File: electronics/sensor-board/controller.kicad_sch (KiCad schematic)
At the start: 22 parts

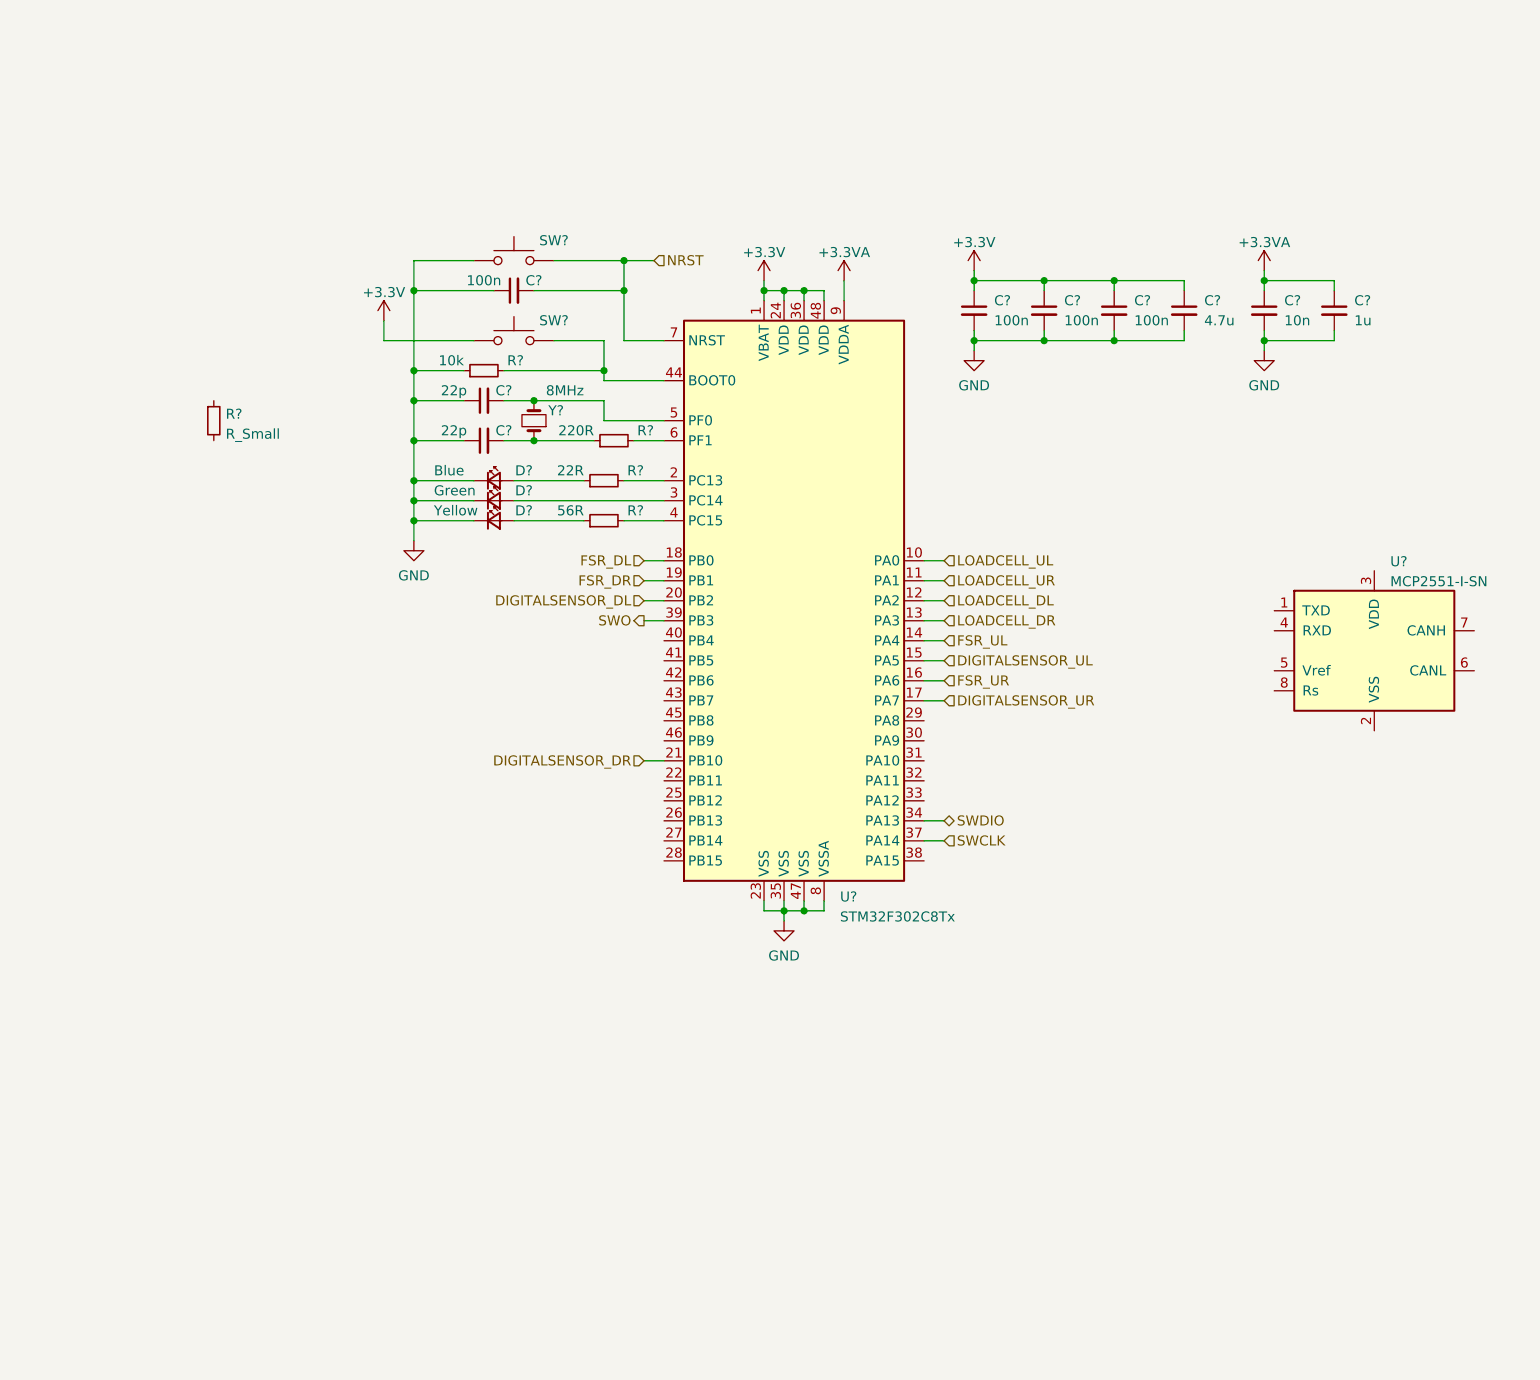
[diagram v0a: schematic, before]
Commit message: Finish microcontroller design + hierarchy
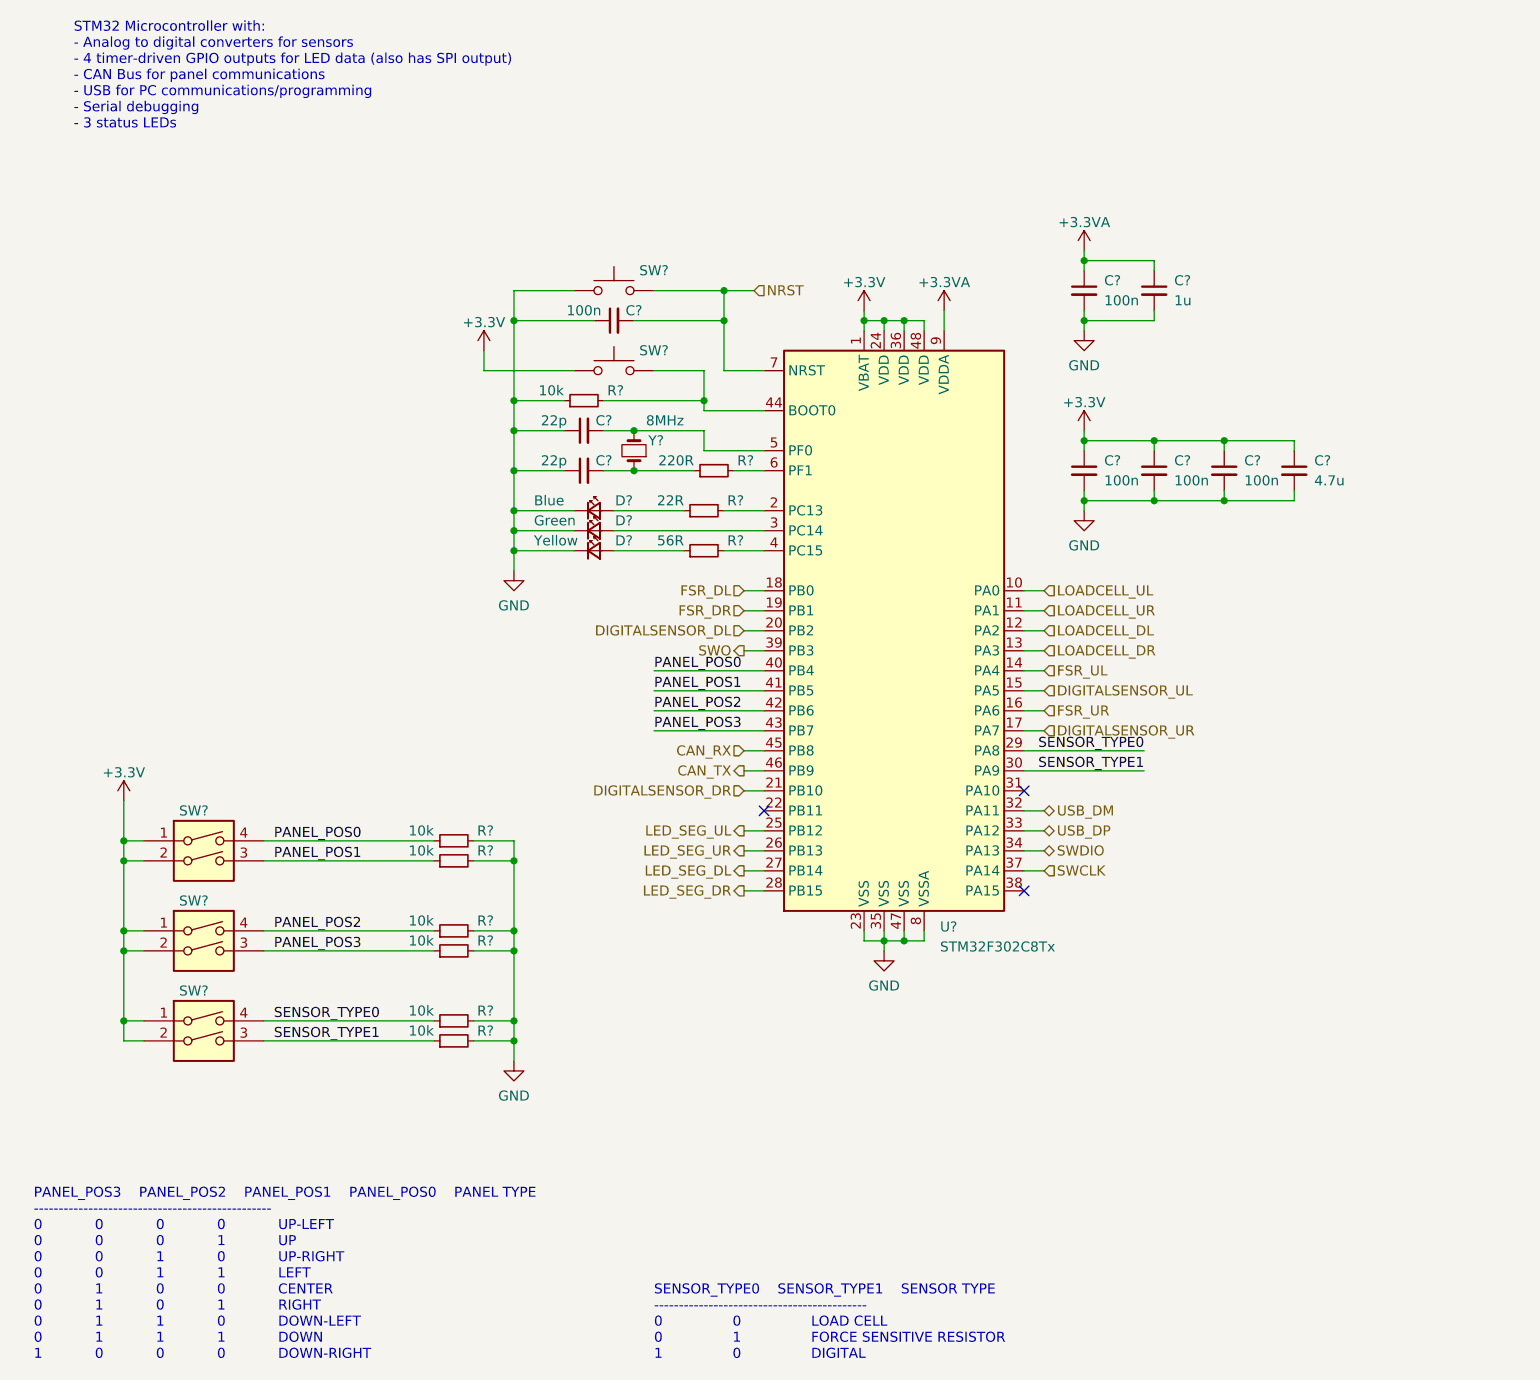
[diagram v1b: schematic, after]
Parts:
- removed R?: R_Small, symbol Device:R_Small
- removed U?: MCP2551-I-SN, Package_SO:SOIC-8_3.9x4.9mm_P1.27mm, symbol Interface_CAN_LIN:MCP2551-I-SN
- added R? (x6): 10k, symbol Device:R_Small
- added SW? (x3): SW_DIP_x02, symbol Switch:SW_DIP_x02
- C?: value 10n -> 100n
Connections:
- net +3.3V: now also SW?.1, SW?.1, SW?.1, SW?.2, SW?.2, SW?.2
- net GND: now also R?.2, R?.2, R?.2, R?.2, R?.2, R?.2
- net LED_SEG_UL: now reaches U?.25 (PB12)
- net LED_SEG_UR: now reaches U?.26 (PB13)
- net LED_SEG_DL: now reaches U?.27 (PB14)
- net LED_SEG_DR: now reaches U?.28 (PB15)
- net SENSOR_TYPE0: now reaches U?.29 (PA8)
- net SENSOR_TYPE0: now also R?.1, SW?.4
- net SENSOR_TYPE1: now reaches U?.30 (PA9)
- net SENSOR_TYPE1: now also R?.1, SW?.3
- net USB_DM: now reaches U?.32 (PA11)
- net USB_DP: now reaches U?.33 (PA12)
- net PANEL_POS0: now reaches U?.40 (PB4)
- net PANEL_POS0: now also R?.1, SW?.4
- net PANEL_POS1: now reaches U?.41 (PB5)
- net PANEL_POS1: now also R?.1, SW?.3
- net PANEL_POS2: now reaches U?.42 (PB6)
- net PANEL_POS2: now also R?.1, SW?.4
- net PANEL_POS3: now reaches U?.43 (PB7)
- net PANEL_POS3: now also R?.1, SW?.3
- net CAN_RX: now reaches U?.45 (PB8)
- net CAN_TX: now reaches U?.46 (PB9)
- no-connect marks 0 -> 3
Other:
- note added: "PANEL_POS3 PANEL_POS2 PANEL_POS1 PANEL_POS0 PANEL TYPE ------------------------------------------------ 0 0 0 0 UP-LEFT 0 0 0 1 UP 0 0 1 0 UP-RIGHT 0 0 1 1 LEFT 0 1 0 0 CENTER 0 1 0 1 RIGHT 0 1 1 0 DOWN-LEFT 0 1 1 1 DOWN 1 0 0 0 DOWN-RIGHT"
- note added: "SENSOR_TYPE0 SENSOR_TYPE1 SENSOR TYPE ------------------------------------------- 0 0 LOAD CELL 0 1 FORCE SENSITIVE RESISTOR 1 0 DIGITAL"
- note added: "STM32 Microcontroller with: - Analog to digital converters for sensors - 4 timer-driven GPIO outputs for LED data (also has SPI output) - CAN Bus for panel communications - USB for PC communications/programming - Serial debugging - 3 status LEDs"
- moved on the sheet: C?, D?, R?, SW?, U?, Y?

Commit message: LED output, debug and minor controller changes
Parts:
- added R? (x2): 10k, symbol Device:R_Small
- added R?: 56R, symbol Device:R_Small
- added SW?: SW_DIP_x02, symbol Switch:SW_DIP_x02
- R?: value 22R -> 47R
- R?: value 56R -> 120R
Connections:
- net +3.3V: now also SW?.1, SW?.2
- net GND: now also R?.2, R?.2
- net at D?.2 (A): now also R?.1; no longer U?.3 (PC14)
- net SENSOR_POS: now reaches U?.22 (PB11)
- net SENSOR_POS: now also R?.1, SW?.4
- net DEBUG: now reaches U?.31 (PA10)
- net DEBUG: now also R?.1, SW?.3
- new net: R?.2, U?.3 (PC14)
- no-connect marks 3 -> 1
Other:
- note added: "PANEL_POS3 PANEL_POS2 PANEL_POS1 PANEL_POS0 PANEL POSITION ------------------------------------------------- 0 0 0 0 UP-LEFT 0 0 0 1 UP 0 0 1 0 UP-RIGHT 0 0 1 1 LEFT 0 1 0 0 CENTER 0 1 0 1 RIGHT 0 1 1 0 DOWN-LEFT 0 1 1 1 DOWN 1 0 0 0 DOWN-RIGHT"
- note added: "SENSOR_POS SENSOR POSITION --------------------- 0 CORNER 1 CARDINAL"
- note removed: "PANEL_POS3 PANEL_POS2 PANEL_POS1 PANEL_POS0 PANEL TYPE ------------------------------------------------ 0 0 0 0 UP-LEFT 0 0 0 1 UP 0 0 1 0 UP-RIGHT 0 0 1 1 LEFT 0 1 0 0 CENTER 0 1 0 1 RIGHT 0 1 1 0 DOWN-LEFT 0 1 1 1 DOWN 1 0 0 0 DOWN-RIGHT"
- moved on the sheet: R?, SW?

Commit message: Build Pad Bus and annotate
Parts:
- gave numbers to parts that had none: 33

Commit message: Minor tweaks, footprints added
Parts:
- added C57: 470n, Capacitor_SMD:C_0603_1608Metric, symbol Device:C_Small
- C29, C30, C31, C32, C33, C35, C36, C37: footprint (none) -> Capacitor_SMD:C_0603_1608Metric
- C34: value 1u -> 470n; footprint (none) -> Capacitor_SMD:C_0603_1608Metric
- D1, D2, D3: footprint (none) -> LED_SMD:LED_0603_1608Metric
- R33, R34, R35, R36, R37, R38, R39, R40, R41, R42, R43, R44, R45: footprint (none) -> Resistor_SMD:R_0603_1608Metric
- SW1, SW2, SW3, SW4: footprint (none) -> Button_Switch_THT:SW_DIP_SPSTx02_Slide_6.7x6.64mm_W7.62mm_P2.54mm_LowProfile
- SW5, SW6: footprint (none) -> sensor-board:TS-1187A-B-A-B
- Y1: footprint (none) -> Crystal:Crystal_SMD_5032-2Pin_5.0x3.2mm
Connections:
- net +3.3VA: now also C57.1
- net GND: now also C57.2

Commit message: Final tweaks and schematic review complete
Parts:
- removed C57: 470n, Capacitor_SMD:C_0603_1608Metric, symbol Device:C_Small
- C34: value 470n -> 1u
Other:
- note added: "DEBUG DEBUG ----------- 0 OFF 1 ON"
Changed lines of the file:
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@@
   (junction (at 67.31 142.24) (diameter 0) (color 0 0 0 0)
   )
-  (junction (at 158.75 59.69) (diameter 0) (color 0 0 0 0)
-  )
   (junction (at 158.75 82.55) (diameter 0) (color 0 0 0 0)
   )
@@
   )
   (junction (at 149.86 74.93) (diameter 0) (color 0 0 0 0)
-  )
-  (junction (at 158.75 52.07) (diameter 0) (color 0 0 0 0)
   )
   (junction (at 92.71 73.66) (diameter 0) (color 0 0 0 0)
@@
     (stroke (width 0) (type default) (color 0 0 0 0))
   )
-  (wire (pts (xy 158.75 59.69) (xy 167.64 59.69))
-    (stroke (width 0) (type default) (color 0 0 0 0))
-  )
   (wire (pts (xy 167.64 82.55) (xy 176.53 82.55))
     (stroke (width 0) (type default) (color 0 0 0 0))
@@
     (stroke (width 0) (type default) (color 0 0 0 0))
   )
-  (wire (pts (xy 167.64 53.34) (xy 167.64 52.07))
-    (stroke (width 0) (type default) (color 0 0 0 0))
-  )
   (wire (pts (xy 158.75 74.93) (xy 167.64 74.93))
     (stroke (width 0) (type default) (color 0 0 0 0))
@@
     (stroke (width 0) (type default) (color 0 0 0 0))
   )
-  (wire (pts (xy 158.75 52.07) (xy 167.64 52.07))
-    (stroke (width 0) (type default) (color 0 0 0 0))
-  )
   (wire (pts (xy 158.75 59.69) (xy 158.75 58.42))
     (stroke (width 0) (type default) (color 0 0 0 0))
@@
   )
   (wire (pts (xy 142.24 121.92) (xy 144.78 121.92))
-    (stroke (width 0) (type default) (color 0 0 0 0))
-  )
-  (wire (pts (xy 167.64 58.42) (xy 167.64 59.69))
     (stroke (width 0) (type default) (color 0 0 0 0))
   )
@@
   (text "PANEL_POS3	PANEL_POS2	PANEL_POS1	PANEL_POS0	PANEL POSITION\n-------------------------------------------------\n0			0        	0			0			UP-LEFT\n0			0			0			1			UP\n0			0			1			0			UP-RIGHT\n0			0			1			1			LEFT\n0			1			0			0			CENTER\n0			1			0			1			RIGHT\n0			1			1			0			DOWN-LEFT\n0			1			1			1			DOWN\n1			0			0			0			DOWN-RIGHT"
     (at 16.51 191.77 0)
+    (effects (font (size 1.27 1.27)) (justify left bottom))
+  )
+  (text "DEBUG	DEBUG\n-----------\n0		OFF\n1		ON" (at 135.89 191.77 0)
     (effects (font (size 1.27 1.27)) (justify left bottom))
   )
@@
       (effects (font (size 1.27 1.27)) (justify left))
     )
-    (property "Value" "470n" (id 1) (at 161.29 57.15 0)
+    (property "Value" "1u" (id 1) (at 161.29 57.15 0)
       (effects (font (size 1.27 1.27)) (justify left))
     )
@@
       (effects (font (size 1.27 1.27)) hide)
     )
-    (pin "1")
-    (pin "2")
-  )
-  (symbol (lib_id "Device:C_Small") (at 167.64 55.88 0) (unit 1)
-    (in_bom yes) (on_board yes)
-    (property "Reference" "C57" (id 0) (at 170.18 54.61 0)
-      (effects (font (size 1.27 1.27)) (justify left))
-    )
-    (property "Value" "470n" (id 1) (at 170.18 57.15 0)
-      (effects (font (size 1.27 1.27)) (justify left))
-    )
-    (property "Footprint" "Capacitor_SMD:C_0603_1608Metric" (id 2) (at 167.64 55.88 0)
-      (effects (font (size 1.27 1.27)) hide)
-    )
-    (property "Datasheet" "~" (id 3) (at 167.64 55.88 0)
-      (effects (font (size 1.27 1.27)) hide)
-    )

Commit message: Set up board rules w/ controlled impedance
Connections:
- net USB_DM renamed USBD_N
- net USB_DP renamed USBD_P
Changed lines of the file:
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@@
     (effects (font (size 1.27 1.27)) (justify right))
   )
-  (hierarchical_label "USB_DP" (shape bidirectional) (at 144.78 124.46 0)
+  (hierarchical_label "USBD_P" (shape bidirectional) (at 144.78 124.46 0)
     (effects (font (size 1.27 1.27)) (justify left))
   )
@@
     (effects (font (size 1.27 1.27)) (justify right))
   )
-  (hierarchical_label "USB_DM" (shape bidirectional) (at 144.78 121.92 0)
+  (hierarchical_label "USBD_N" (shape bidirectional) (at 144.78 121.92 0)
     (effects (font (size 1.27 1.27)) (justify left))
   )

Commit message: Remove DIP switches and re-organize CAN connectors
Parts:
- removed R33, R34, R35, R36, R37, R38, R39, R40: 10k, Resistor_SMD:R_0603_1608Metric, symbol Device:R_Small
- removed SW1, SW2, SW3, SW4: SW_DIP_x02, Button_Switch_THT:SW_DIP_SPSTx02_Slide_6.7x6.64mm_W7.62mm_P2.54mm_LowProfile, symbol Switch:SW_DIP_x02
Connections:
- net DEBUG: no longer names the net of U9.31 (PA10)
- net PANEL_POS0: no longer names the net of U9.40 (PB4)
- net PANEL_POS1: no longer names the net of U9.41 (PB5)
- net PANEL_POS2: no longer names the net of U9.42 (PB6)
- net PANEL_POS3: no longer names the net of U9.43 (PB7)
- net SENSOR_POS renamed LED_EN
- net SENSOR_TYPE0: no longer names the net of U9.29 (PA8)
- net SENSOR_TYPE1: no longer names the net of U9.30 (PA9)
- no-connect marks 1 -> 8
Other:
- note removed: "DEBUG DEBUG ----------- 0 OFF 1 ON"
- note removed: "PANEL_POS3 PANEL_POS2 PANEL_POS1 PANEL_POS0 PANEL POSITION ------------------------------------------------- 0 0 0 0 UP-LEFT 0 0 0 1 UP 0 0 1 0 UP-RIGHT 0 0 1 1 LEFT 0 1 0 0 CENTER 0 1 0 1 RIGHT 0 1 1 0 DOWN-LEFT 0 1 1 1 DOWN 1 0 0 0 DOWN-RIGHT"
- note removed: "SENSOR_POS SENSOR POSITION --------------------- 0 CORNER 1 CARDINAL"
- note removed: "SENSOR_TYPE0 SENSOR_TYPE1 SENSOR TYPE ------------------------------------------- 0 0 LOAD CELL 0 1 FORCE SENSITIVE RESISTOR 1 0 DIGITAL"
